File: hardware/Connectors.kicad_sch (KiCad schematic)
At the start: 23 parts, among them J1 USB_C_Receptacle_USB2.0, J14 Conn_01x05, J2 M80-5302642, J3 M300-MV31045M1, J4 M80-5L10442MC, J5 M80-5L10442MC, J6 M80-5L10442MC, J8 M80-5L10642MC

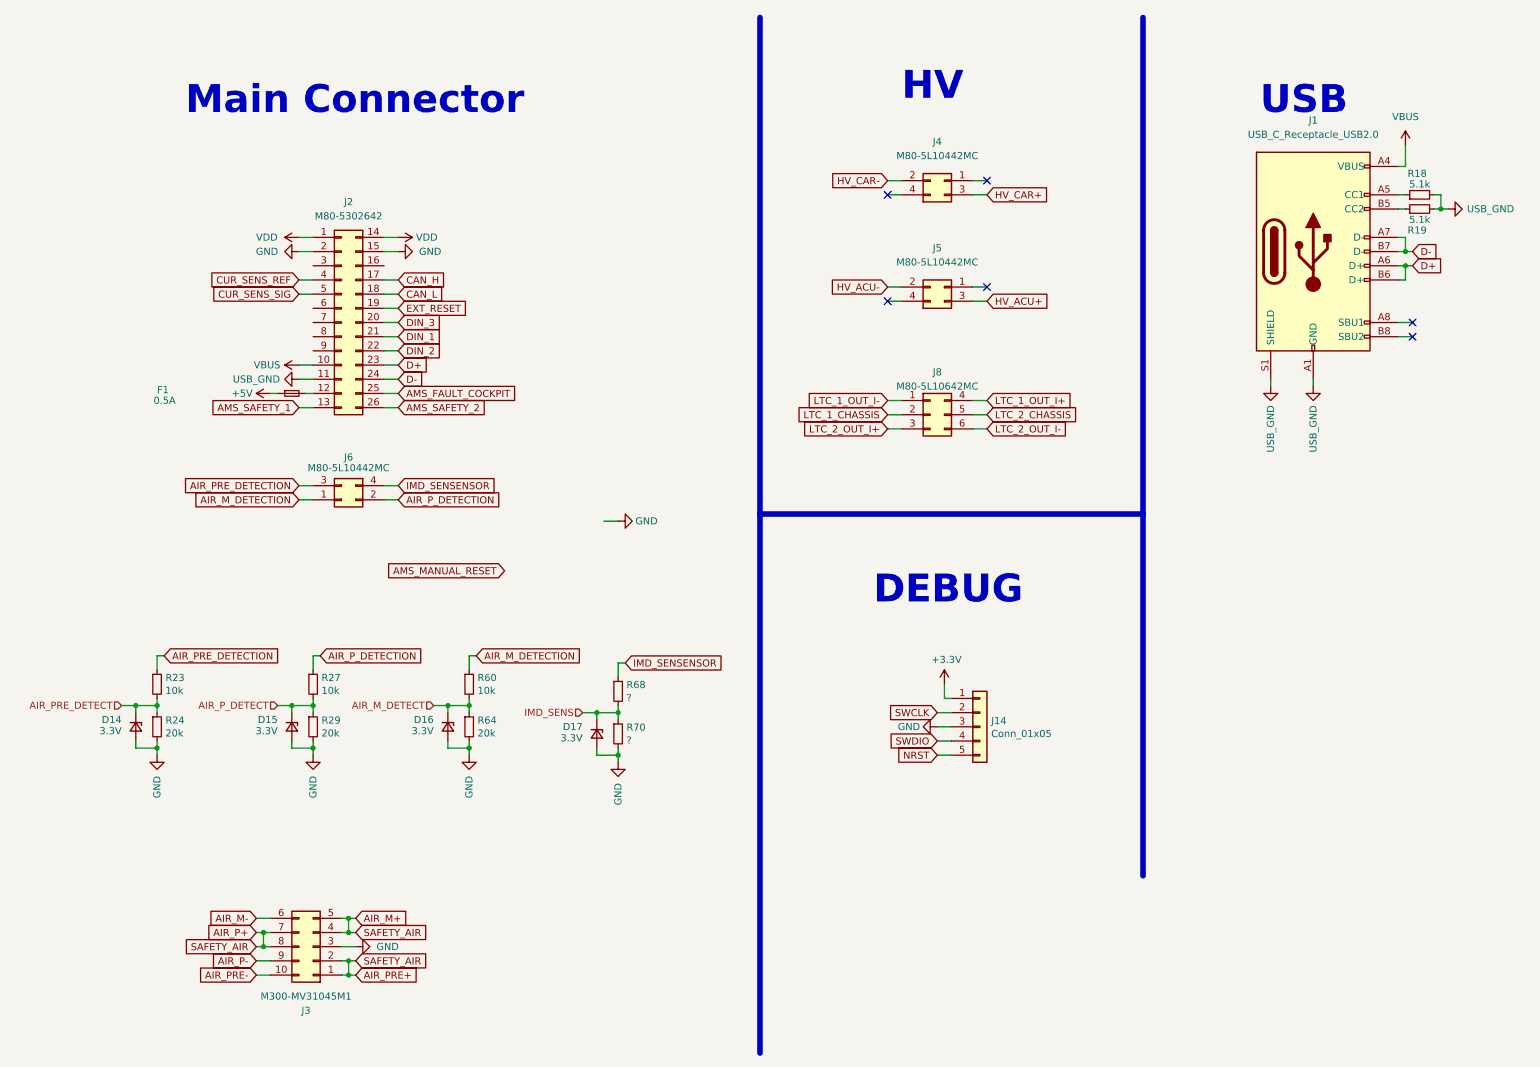
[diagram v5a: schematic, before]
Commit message: major changes: conn, fans, inputs and others
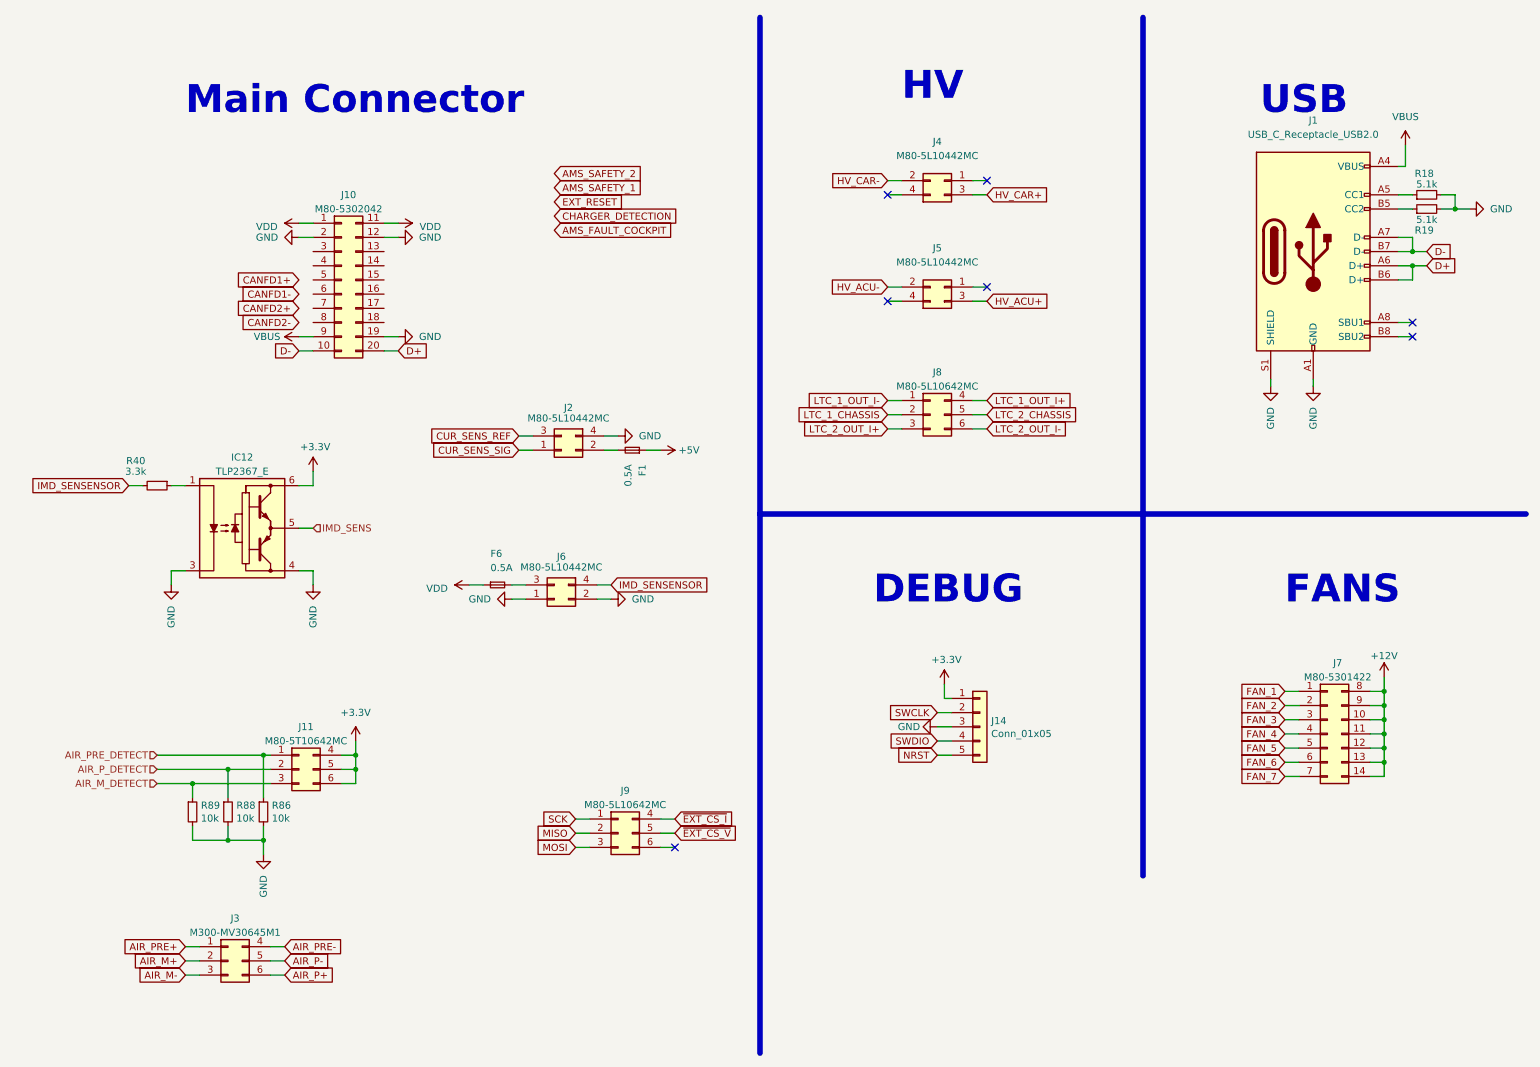
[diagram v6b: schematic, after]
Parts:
- removed D14, D15, D16, D17: 3.3V, Diode_SMD:D_SOD-323_HandSoldering, symbol Device:D_Zener_Small
- removed J2: M80-5302642, M80-53026YY, symbol M80-5302642:M80-5302642
- removed J3: M300-MV31045M1, M300MV31045M1, symbol M300-MV31045M1:M300-MV31045M1
- removed R23, R27, R60: 10k, Resistor_SMD:R_0603_1608Metric, symbol Device:R_Small
- removed R24, R29, R64: 20k, Resistor_SMD:R_0603_1608Metric, symbol Device:R_Small
- removed R68, R70: ?, Resistor_SMD:R_0603_1608Metric, symbol Device:R_Small
- added F6: 0.5A, Fuse:Fuse_1206_3216Metric, symbol Device:Fuse_Small
- added IC12: TLP2367_E, TLP2367:SOIC127P700X220-6N, symbol TLP2367_E:TLP2367_E
- added J10: M80-5302042, M80-5302042:M80-53020YY, symbol M80-5302042:M80-5302042
- added J11: M80-5T10642MC, M80-5T1062MC:M80-5T106YYMC, symbol M80-5T10642MC:M80-5T10642MC
- added J2: M80-5L10442MC, M80-5L104YYMC, symbol M80-5L10442MC:M80-5L10442MC
- added J3: M300-MV30645M1, M300-MV30645M1:M300MV30645M1, symbol M300-MV30645M1:M300-MV30645M1
- added J7: M80-5301422, M80-5301422:M80-53014YY, symbol M80-5301422:M80-5301422
- added J9: M80-5L10642MC, M80-5L10642MC:M80-5L106YYMC, symbol M80-5L10642MC:M80-5L10642MC
- added R40: 3.3k, Resistor_SMD:R_0603_1608Metric, symbol Device:R_Small
- added R86, R88, R89: 10k, Resistor_SMD:R_0603_1608Metric, symbol Device:R_Small
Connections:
- net AIR_M_DETECTION is gone; now on net GND: J6.1
- net AIR_P_DETECTION is gone; now on net GND: J6.2
- net USB_GND is gone; now on net GND: J1.A1 (GND), J1.A12 (GND), J1.B1 (GND), J1.B12 (GND), J1.S1 (SHIELD), R18.2, R19.2
- net +3V3: now also IC12.6, J11.4, J11.5, J11.6
- net AIR_M+: now also J3.2
- net AIR_M-: now also J3.3
- net AIR_M_DETECT: now also J11.3, R89.1
- net AIR_P-: now also J3.5
- net AIR_PRE-: now also J3.4
- net AIR_PRE_DETECT: now also J11.1, R86.1
- net AIR_P_DETECT: now also J11.2, R88.1
- net CUR_SENS_REF: now also J2.3
- net CUR_SENS_SIG: now also J2.1
- net D+: now also J10.20
- net D-: now also J10.10
- net GND: now also IC12.3, IC12.4, J10.12, J10.19, J10.2, J2.4, R86.2, R88.2, R89.2
- net IMD_SENS: now also IC12.5
- net IMD_SENSENSOR: now also R40.2
- net VBUS: now also J10.9
- net VDD: now also F6.1, J10.1, J10.11
- net at F1.2: now also J2.2
- net AIR_PRE_DETECTION: no longer names the net of J6.3
- net AIR_PRE_DETECTION: now also F6.2
- new net: IC12.1, R40.1
- new net +12V: J7.10, J7.11, J7.12, J7.13, J7.14, J7.8, J7.9
- new net AIR_P+: J3.6
- new net AIR_PRE+: J3.1
- new net FAN_1: J7.1
- new net FAN_2: J7.2
- new net FAN_3: J7.3
- new net FAN_4: J7.4
- new net FAN_5: J7.5
- new net FAN_6: J7.6
- new net FAN_7: J7.7
- new net MISO: J9.2
- new net MOSI: J9.3
- new net SCK: J9.1
- new net ~{EXT_CS_I}: J9.4
- new net ~{EXT_CS_V}: J9.5
- no-connect marks 6 -> 7
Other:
- note added: "FANS"
- moved on the sheet: F1, J6, R18, R19

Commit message: further improvements
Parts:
- removed IC12: TLP2367_E, TLP2367:SOIC127P700X220-6N, symbol TLP2367_E:TLP2367_E
- removed J11: M80-5T10642MC, M80-5T1062MC:M80-5T106YYMC, symbol M80-5T10642MC:M80-5T10642MC
- removed R40: 3.3k, Resistor_SMD:R_0603_1608Metric, symbol Device:R_Small
- removed R86, R88, R89: 10k, Resistor_SMD:R_0603_1608Metric, symbol Device:R_Small
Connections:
- net AIR_P+ is gone; now on net SAFETY_TSMS_IN: J3.6
- net AIR_PRE+ is gone; now on net SAFETY_TSMS_IN: J3.1
- net CANFD1+: now also J10.7
- net CANFD1-: now also J10.6
- net CANFD2+: now also J10.5
- net CANFD2-: now also J10.4
- net D+: now also J10.9; no longer J10.20
- net D-: now also J10.8; no longer J10.10
- net GND: now also J10.18; no longer J10.19
- net IMD_SENSENSOR: now also J6.3; no longer J6.4
- net VBUS: now also J10.19; no longer J10.9
- net at F6.2: now also J6.4; no longer J6.3
- net AIR_M+ renamed SAFETY_TSMS_IN
- net SAFETY_TSMS_IN: now also J10.10, J10.20
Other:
- moved on the sheet: F1, F6, J2, J6, J9

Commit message: PCB routing 50-70% done
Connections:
- net LTC_2_CHASSIS is gone; now on net LTC_CHASSIS: J8.5
- net AMS_FAULT_COCKPIT: now also J10.13
- net AMS_SAFETY_1: now also J10.3
- net AMS_SAFETY_2: now also J10.14
- net CANFD1+: now also J10.9; no longer J10.7
- net CANFD1-: now also J10.8; no longer J10.6
- net CANFD2+: now also J10.7; no longer J10.5
- net CANFD2-: now also J10.6; no longer J10.4
- net D+: now also J10.16; no longer J10.9
- net D-: now also J10.17; no longer J10.8
- net EXT_RESET: now also J10.4
- net LTC_1_CHASSIS renamed LTC_CHASSIS
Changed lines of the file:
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@@
+    (stroke (width 0) (type default))
+  )
+  (wire (pts (xy 64.77 69.85) (xy 67.31 69.85))
     (stroke (width 0) (type default))
   )
@@
     (stroke (width 0) (type default))
   )
+  (wire (pts (xy 64.77 54.61) (xy 67.31 54.61))
+    (stroke (width 0) (type default))
+  )
   (wire (pts (xy 170.18 63.5) (xy 172.72 63.5))
     (stroke (width 0) (type default))
@@
     (stroke (width 0) (type default))
   )
-  (wire (pts (xy 64.77 69.85) (xy 67.31 69.85))
+  (wire (pts (xy 82.55 64.77) (xy 80.01 64.77))
     (stroke (width 0) (type default))
   )
@@
     (stroke (width 0) (type default))
   )
+  (wire (pts (xy 82.55 57.15) (xy 80.01 57.15))
+    (stroke (width 0) (type default))
+  )
   (wire (pts (xy 59.69 179.07) (xy 62.23 179.07))
     (stroke (width 0) (type default))
@@
     (stroke (width 0) (type default))
   )
+  (wire (pts (xy 64.77 57.15) (xy 67.31 57.15))
+    (stroke (width 0) (type default))
+  )
   (wire (pts (xy 181.61 137.16) (xy 179.07 137.16))
     (stroke (width 0) (type default))
@@
   )
   (wire (pts (xy 261.62 39.37) (xy 262.89 39.37))
+    (stroke (width 0) (type default))
+  )
+  (wire (pts (xy 64.77 62.23) (xy 67.31 62.23))
     (stroke (width 0) (type default))
   )
@@
     (stroke (width 0) (type default))
   )
-  (wire (pts (xy 64.77 67.31) (xy 67.31 67.31))
+  (wire (pts (xy 82.55 62.23) (xy 80.01 62.23))
     (stroke (width 0) (type default))
   )
@@
   )
   (wire (pts (xy 80.01 52.07) (xy 82.55 52.07))
+    (stroke (width 0) (type default))
+  )
+  (wire (pts (xy 80.01 54.61) (xy 82.55 54.61))
     (stroke (width 0) (type default))
   )
@@
     (stroke (width 0) (type default))
   )
+  (wire (pts (xy 64.77 64.77) (xy 67.31 64.77))
+    (stroke (width 0) (type default))
+  )
   (wire (pts (xy 185.42 41.91) (xy 187.96 41.91))
     (stroke (width 0) (type default))
@@
   )
   (wire (pts (xy 243.84 146.05) (xy 241.3 146.05))
+    (stroke (width 0) (type default))
+  )
+  (wire (pts (xy 64.77 67.31) (xy 67.31 67.31))
     (stroke (width 0) (type default))
   )
@@
     )
   )
-  (global_label "CANFD2+" (shape input) (at 67.31 59.69 180) (fields_autoplaced)
-    (effects (font (size 1.27 1.27)) (justify right))
-    (property "Intersheetrefs" "${INTERSHEET_REFS}" (at 56.2288 59.69 0)
+  (global_label "CANFD2+" (shape input) (at 64.77 64.77 180) (fields_autoplaced)
+    (effects (font (size 1.27 1.27)) (justify right))
+    (property "Intersheetrefs" "${INTERSHEET_REFS}" (at 53.6888 64.77 0)
       (effects (font (size 1.27 1.27)) (justify right) hide)
     )
@@
     )
   )
-  (global_label "LTC_1_CHASSIS" (shape input) (at 170.18 83.82 180) (fields_autoplaced)
-    (effects (font (size 1.27 1.27)) (justify right))
-    (property "Intersheetrefs" "${INTERSHEET_REFS}" (at 153.5956 83.82 0)
+  (global_label "LTC_CHASSIS" (shape input) (at 170.18 83.82 180) (fields_autoplaced)
+    (effects (font (size 1.27 1.27)) (justify right))
+    (property "Intersheetrefs" "${INTERSHEET_REFS}" (at 155.7727 83.82 0)
       (effects (font (size 1.27 1.27)) (justify right) hide)
     )
@@
     )
   )
-  (global_label "CANFD1+" (shape input) (at 67.31 64.77 180) (fields_autoplaced)
-    (effects (font (size 1.27 1.27)) (justify right))
-    (property "Intersheetrefs" "${INTERSHEET_REFS}" (at 56.2288 64.77 0)
+  (global_label "CANFD1+" (shape input) (at 64.77 69.85 180) (fields_autoplaced)
+    (effects (font (size 1.27 1.27)) (justify right))
+    (property "Intersheetrefs" "${INTERSHEET_REFS}" (at 53.6888 69.85 0)
       (effects (font (size 1.27 1.27)) (justify right) hide)
     )
@@
     )
   )
-  (global_label "CANFD1-" (shape input) (at 67.31 62.23 180) (fields_autoplaced)
-    (effects (font (size 1.27 1.27)) (justify right))
-    (property "Intersheetrefs" "${INTERSHEET_REFS}" (at 56.2288 62.23 0)
+  (global_label "CANFD1-" (shape input) (at 64.77 67.31 180) (fields_autoplaced)
+    (effects (font (size 1.27 1.27)) (justify right))
+    (property "Intersheetrefs" "${INTERSHEET_REFS}" (at 53.6888 67.31 0)
       (effects (font (size 1.27 1.27)) (justify right) hide)
     )
@@
     )
   )
-  (global_label "EXT_RESET" (shape input) (at 110.49 45.72 0) (fields_autoplaced)
-    (effects (font (size 1.27 1.27)) (justify left))
-    (property "Intersheetrefs" "${INTERSHEET_REFS}" (at 122.7804 45.72 0)
-      (effects (font (size 1.27 1.27)) (justify left) hide)
-    )
-  )
-  (global_label "AMS_FAULT_COCKPIT" (shape input) (at 110.49 50.8 0) (fields_autoplaced)
-    (effects (font (size 1.27 1.27)) (justify left))
-    (property "Intersheetrefs" "${INTERSHEET_REFS}" (at 131.9126 50.8 0)
+  (global_label "EXT_RESET" (shape input) (at 64.77 57.15 180) (fields_autoplaced)
+    (effects (font (size 1.27 1.27)) (justify right))
+    (property "Intersheetrefs" "${INTERSHEET_REFS}" (at 52.4796 57.15 0)
+      (effects (font (size 1.27 1.27)) (justify right) hide)
+    )
+  )
+  (global_label "AMS_FAULT_COCKPIT" (shape input) (at 82.55 54.61 0) (fields_autoplaced)
+    (effects (font (size 1.27 1.27)) (justify left))
+    (property "Intersheetrefs" "${INTERSHEET_REFS}" (at 103.9726 54.61 0)
       (effects (font (size 1.27 1.27)) (justify left) hide)
     )
@@
     )
   )
-  (global_label "CHARGER_DETECTION" (shape input) (at 110.49 48.26 0) (fields_autoplaced)
-    (effects (font (size 1.27 1.27)) (justify left))
-    (property "Intersheetrefs" "${INTERSHEET_REFS}" (at 132.3963 48.26 0)
+  (global_label "CHARGER_DETECTION" (shape input) (at 114.3 62.23 0) (fields_autoplaced)
+    (effects (font (size 1.27 1.27)) (justify left))
+    (property "Intersheetrefs" "${INTERSHEET_REFS}" (at 136.2063 62.23 0)
       (effects (font (size 1.27 1.27)) (justify left) hide)
     )
@@
     )
   )
-  (global_label "AMS_SAFETY_2" (shape input) (at 110.49 40.64 0) (fields_autoplaced)
-    (effects (font (size 1.27 1.27)) (justify left))
-    (property "Intersheetrefs" "${INTERSHEET_REFS}" (at 126.2277 40.64 0)
+  (global_label "AMS_SAFETY_2" (shape input) (at 82.55 57.15 0) (fields_autoplaced)
+    (effects (font (size 1.27 1.27)) (justify left))
+    (property "Intersheetrefs" "${INTERSHEET_REFS}" (at 98.2877 57.15 0)
       (effects (font (size 1.27 1.27)) (justify left) hide)
     )
@@
     )
   )
-  (global_label "AMS_SAFETY_1" (shape input) (at 110.49 43.18 0) (fields_autoplaced)
-    (effects (font (size 1.27 1.27)) (justify left))
-    (property "Intersheetrefs" "${INTERSHEET_REFS}" (at 126.2277 43.18 0)
-      (effects (font (size 1.27 1.27)) (justify left) hide)
-    )
-  )
-  (global_label "D+" (shape input) (at 64.77 69.85 180) (fields_autoplaced)
-    (effects (font (size 1.27 1.27)) (justify right))
-    (property "Intersheetrefs" "${INTERSHEET_REFS}" (at 59.676 69.85 0)
-      (effects (font (size 1.27 1.27)) (justify right) hide)
+  (global_label "AMS_SAFETY_1" (shape input) (at 64.77 54.61 180) (fields_autoplaced)
+    (effects (font (size 1.27 1.27)) (justify right))
+    (property "Intersheetrefs" "${INTERSHEET_REFS}" (at 49.0323 54.61 0)
+      (effects (font (size 1.27 1.27)) (justify right) hide)
+    )
+  )
+  (global_label "D+" (shape input) (at 82.55 62.23 0) (fields_autoplaced)
+    (effects (font (size 1.27 1.27)) (justify left))
+    (property "Intersheetrefs" "${INTERSHEET_REFS}" (at 87.644 62.23 0)
+      (effects (font (size 1.27 1.27)) (justify left) hide)
     )
   )
@@
     )
   )
+  (global_label "BOOT0" (shape input) (at 121.92 71.12 0) (fields_autoplaced)
+    (effects (font (size 1.27 1.27)) (justify left))
+    (property "Intersheetrefs" "${INTERSHEET_REFS}" (at 26.67 -26.67 0)
+      (effects (font (size 1.27 1.27)) hide)
+    )
+  )
   (global_label "D+" (shape input) (at 266.7 57.15 0) (fields_autoplaced)
     (effects (font (size 1.27 1.27)) (justify left))
@@
     )
   )
-  (global_label "CANFD2-" (shape input) (at 67.31 57.15 180) (fields_autoplaced)
-    (effects (font (size 1.27 1.27)) (justify right))
-    (property "Intersheetrefs" "${INTERSHEET_REFS}" (at 56.2288 57.15 0)
+  (global_label "CANFD2-" (shape input) (at 64.77 62.23 180) (fields_autoplaced)
+    (effects (font (size 1.27 1.27)) (justify right))
+    (property "Intersheetrefs" "${INTERSHEET_REFS}" (at 53.6888 62.23 0)
       (effects (font (size 1.27 1.27)) (justify right) hide)
     )
@@
     )
   )
+  (global_label "LTC_CHASSIS" (shape input) (at 187.96 83.82 0) (fields_autoplaced)
+    (effects (font (size 1.27 1.27)) (justify left))
+    (property "Intersheetrefs" "${INTERSHEET_REFS}" (at 202.3673 83.82 0)
+      (effects (font (size 1.27 1.27)) (justify left) hide)
+    )
+  )
   (global_label "LTC_1_OUT_I+" (shape input) (at 187.96 81.28 0) (fields_autoplaced)
     (effects (font (size 1.27 1.27)) (justify left))
@@
     )
   )
-  (global_label "D-" (shape input) (at 64.77 67.31 180) (fields_autoplaced)
-    (effects (font (size 1.27 1.27)) (justify right))
-    (property "Intersheetrefs" "${INTERSHEET_REFS}" (at 59.676 67.31 0)
-      (effects (font (size 1.27 1.27)) (justify right) hide)
-    )
-  )
-  (global_label "LTC_2_CHASSIS" (shape input) (at 187.96 83.82 0) (fields_autoplaced)
-    (effects (font (size 1.27 1.27)) (justify left))
-    (property "Intersheetrefs" "${INTERSHEET_REFS}" (at 204.5444 83.82 0)
-      (effects (font (size 1.27 1.27)) (justify left) hide)
-    )
+  (global_label "D-" (shape input) (at 82.55 64.77 0) (fields_autoplaced)
+    (effects (font (size 1.27 1.27)) (justify left))
+    (property "Intersheetrefs" "${INTERSHEET_REFS}" (at 87.644 64.77 0)
+      (effects (font (size 1.27 1.27)) (justify left) hide)
+    )
